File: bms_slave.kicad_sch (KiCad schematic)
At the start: 0 parts

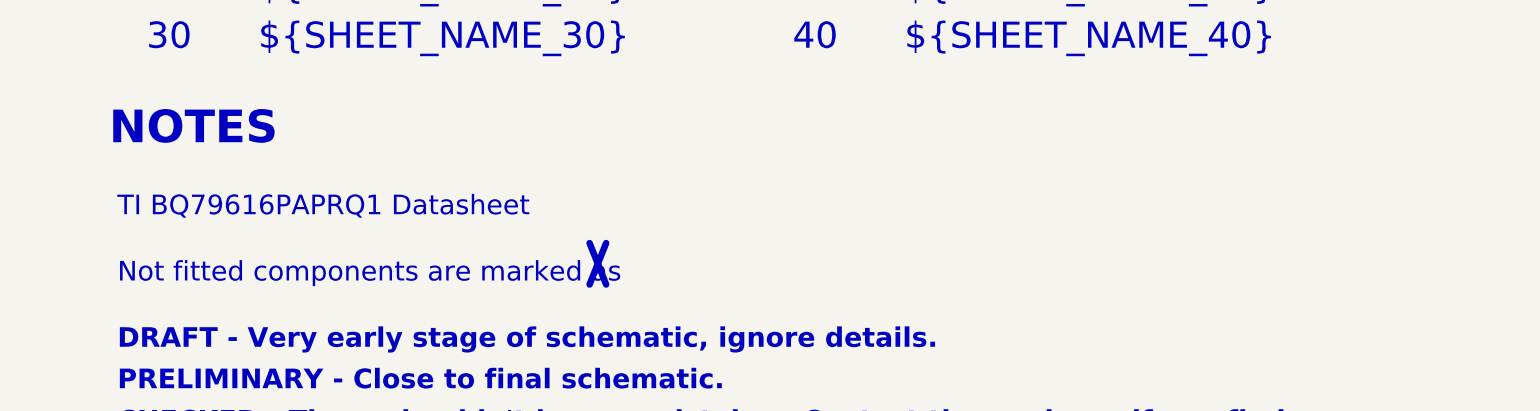
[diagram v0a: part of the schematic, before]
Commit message: PCB[Trace Size, Testpad, Daisy]: Changed Bat Trace size FAT, Made test pads larger, small trace movement to clean up, daisy trace change. SCH[Notes]: Small notes changes.
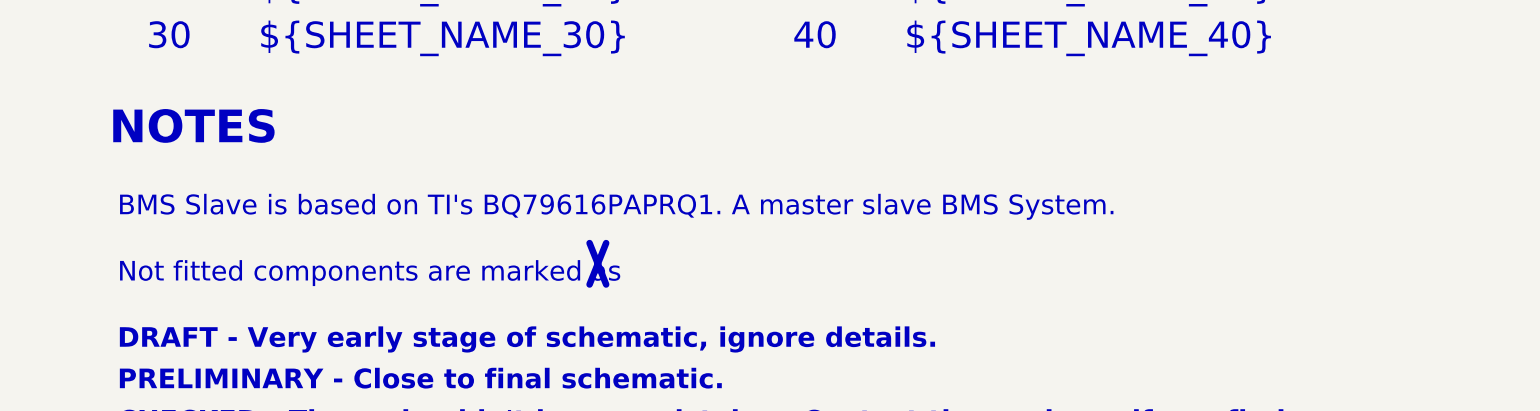
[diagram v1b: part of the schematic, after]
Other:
- note added: "BMS Slave is based on TI's BQ79616PAPRQ1. A master slave BMS System."
- note removed: "TI BQ79616PAPRQ1 Datasheet"
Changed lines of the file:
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@@
 	(paper "A3")
 	(title_block
+		(date "2026-10-28")
 		(rev "${REVISION}")
 		(company "${COMPANY}")
@@
 		)
 	)
-	(text "TI BQ79616PAPRQ1 Datasheet"
+	(text "BMS Slave is based on TI's BQ79616PAPRQ1. A master slave BMS System."
 		(exclude_from_sim no)
 		(at 222.25 177.8 0)
